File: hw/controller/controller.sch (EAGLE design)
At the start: 57 parts, among them J1 MF-CON-MICROUSB-RIGHT, P1 B6B-PH-SM4-TB(LF)(SN), Q1 TPN1R603PL, Q2 TPN1R603PL, Q3 TPN1R603PL, Q4 TPN1R603PL, Q5 TPN1R603PL, Q6 TPN1R603PL, U1 STM32F4R_64PIN, U2 DRV8323RS, U3 AS5147, U4 MAX13431E

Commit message: Checkpoint of controller board layout after much pin assignment
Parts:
- removed P1: B6B-PH-SM4-TB(LF)(SN), controller:B6B-PH-SM4-TB(LF)(SN)
- added D2: MF-LED-0603-GREEN, mfleds:LED_SINGLE-0603-GREEN
- added D3: MF-LED-0603-RED, mfleds:LED_SINGLE-0603-RED
- added J2: JST-ZH6, controller:JST-ZH6
- added J3, J6: PAD4, controller:PAD4
- added J4: JST-PH3SMT_VERT, controller:JST-PH3SMT_VERT
- added J5: PAD2, controller:PAD2
- added R5: 10k, mfpassives:RESISTOR_0603
- added R6, R9: 220, mfpassives:RESISTOR_0603
- J1: value MF-CON-MICROUSB-RIGHT -> JST-PH3SMT_VERT; device mfconnectors:USB_MICRO_RIGHT -> controller:JST-PH3SMT_VERT
- R3: value (none) -> 33.2k 1%; MF (none) -> Panasonic; MPN (none) -> ERJ-3EKF3322V
- R4: value (none) -> 10k 1%; MF (none) -> Panasonic; MPN (none) -> P10.0KHCT-ND
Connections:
- removed net N$1: J1.5V, U1.PA9/TIM1_2/SPI2_SCK/I2S3_CK/UART1_TX/USB_VBUS
- removed net N$3: J1.D+, U1.PA12/USART1_RTS/USB_DP
- removed net N$38: R7.P$1, R8.P$2, U1.PA0WKUP/TIM2_1/TIM5_1/UART4_TX
- removed net N$4: J1.D-, U1.PA11/TIM1_4/USB_DM
- new net I2C_ABS_SCL: J3.3, U1.PB8/TIM2_1/TIM4_3/TIM10_1/I2C1_SCL
- new net I2C_ABS_SDA: J3.2, U1.PB9/TIM2_2/TIM4_4/TIM11_1/I2C1_SDA
- new net LED1: D3.CATHODE, U1.PA11/TIM1_4/USB_DM
- new net LED2: D2.CATHODE, U1.PA12/USART1_RTS/USB_DP
- new net N$15: J1.1, J4.1, U4.A
- new net N$17: D3.ANODE, R6.P$2
- new net N$18: D2.ANODE, R9.P$2
- new net N$9: J1.2, J4.2, U4.B
- new net VBAT_SENSE: R7.P$1, R8.P$2, U1.PC1/SPI3_MOSI/I2S3_SD/SPI2_MOSI/I2S2_SD
- new net VTEMP: J5.2, R5.P$1, U1.PC0
- net +3V3: now also J2.6, J3.1, J5.1, J6.1, R6.P$1, R9.P$1; no longer P1.6
- net AS5047_A: now also U1.PC6/TIM3_1/TIM8_1/I2S2_MCK/UART6_RX
- net AS5047_B: now also U1.PC7/TIM3_2/TIM8_2/SPI2_SCK/I2S2_CK/I2S3_MCK/UART6_RX
- net AS5047_CS: now also U1.PB12; no longer U1.PC15
- net AS5047_MISO: now also U1.PB14/TIM1_2N/TIM8_2N/SPI2_MISO/TIM12_1/USB_HS_DM; no longer U1.PC11/SPI3_MISO/UART3_RX/UART4_RX
- net AS5047_MOSI: now also U1.PB15/TIM1_3N/TIM8_3N/SPI2_MOSI/I2S2_SD/TIM12_2/USB_HS_DP; no longer U1.PC12/I2C2_SDA/SPI3_MOSI/I2S3_SD/UART3_CK/UART5_TX
- net AS5047_SCK: now also U1.PB13/TIM1_1N/SPI2_SCK/I2S2_CK; no longer U1.PC10/SPI3_SCK/I2S3_CK/UART3_TX/UART4_TX
- net CUR1: now also U1.PC4/I2S1_MCK; no longer U1.PC0
- net CUR2: now also U1.PC5/UART3_RX; no longer U1.PC1/SPI3_MOSI/I2S3_SD/SPI2_MOSI/I2S2_SD
- net CUR3: now also U1.PB0/TIM1_2N/TIM3_3/TIM8_2N/SPI3_MOSI/I2S3_SD/UART4_CTS; no longer U1.PC2/SPI2_MISO
- net DEBUG_RX: now also J6.3, U1.PC11/SPI3_MISO/UART3_RX/UART4_RX; no longer U1.PA3/TIM2_4/TIM5_4/TIM9_2/UART2_RX
- net DEBUG_TX: now also J6.2, U1.PC10/SPI3_SCK/I2S3_CK/UART3_TX/UART4_TX; no longer U1.PA2/TIM2_3/TIM5_3/TIM9_1/UART2_TX
- net DRV8323_CS: now also U1.PA4; no longer U1.PA8/TIM1_1/I2C3_SCL
- net GND: now also J1.3, J2.4, J3.4, J4.3, J6.4, R5.P$2; no longer J1.GND, J1.SLD, P1.4
- net MOTOR1: now also U1.PA0WKUP/TIM2_1/TIM5_1/UART4_TX; no longer U1.PC6/TIM3_1/TIM8_1/I2S2_MCK/UART6_RX
- net MOTOR2: now also U1.PA1/TIM2_2/TIM5_2/UART4_RX; no longer U1.PC7/TIM3_2/TIM8_2/SPI2_SCK/I2S2_CK/I2S3_MCK/UART6_RX
- net MOTOR3: now also U1.PA2/TIM2_3/TIM5_3/TIM9_1/UART2_TX; no longer U1.PC8/TIM3_3/TIM8_3/UART6_CK
- net MOTOR_ENABLE: now also U1.PA3/TIM2_4/TIM5_4/TIM9_2/UART2_RX; no longer U1.PC13
- net MOTOR_FAULT: now also U1.PB1/TIM1_3N/TIM3_4/TIM8_3N; no longer U1.PD2
- net MOTOR_HIZ: now also U1.PC3/SPI2_MOSI/I2S2_SD; no longer U1.PC14
- net N$24: now also J2.2; no longer P1.2
- net N$6: now also J2.5; no longer P1.5
- net N$7: now also J2.3; no longer P1.3
- net RS485_DIR: now also U1.PA8/TIM1_1/I2C3_SCL; no longer U1.PB5/TIM3_2/SPI1_MOSI/I2S1_SD/SPI3_MOSI/I2S3_SD
- net RS485_RX: now also U1.PA10/TIM1_3/USART1_RX; no longer U1.PB7/TIM4_2/I2C1_SDA/UART1_RX
- net RS485_TX: now also U1.PA9/TIM1_2/SPI2_SCK/I2S3_CK/UART1_TX/USB_VBUS; no longer U1.PB6/TIM4_1/I2C1_SCL/UART1_TX
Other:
- moved on the sheet: R7, R8

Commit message: Checkpoint after fixing board consistency errors
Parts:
- C4: device mfpassives:CAPACITOR_NP_0603 -> mfpassives:CAPACITOR_NP_0402
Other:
- moved on the sheet: R1, R2, R3, R4, R5, R6, R7, R8, R9

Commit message: Everything nominally placed within the board outline
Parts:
- added C26: 0.1uF, mfpassives:CAPACITOR_NP_0402
- added C27: 1uF, mfpassives:CAPACITOR_NP_0402
- added U$1, U$2, U$3, U$4: MOUNTM2, controller:MOUNTM2
- C10, C11, C12, C13, C2, C21, C23, C24, C25, C3, C5, C6, C8, C9: device mfpassives:CAPACITOR_NP_0603 -> mfpassives:CAPACITOR_NP_0402
- C4: HOUSEPART (none) -> 1; MPN MF-CAP-0603-0.1uF -> MF-CAP-0402-0.1uF
- R1, R2, R5, R6, R9: device mfpassives:RESISTOR_0603 -> mfpassives:RESISTOR_0402
- X1: value (none) -> 8.0MHz
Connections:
- removed net N$2: C13.P$1, C23.P$1, U2.VDRAIN, U2.VM
- net +3V3: now also C26.P$1, C27.P$1
- net GND: now also C26.P$2, C27.P$2
- net V+: now also C13.P$1, C23.P$1, U2.VDRAIN, U2.VM

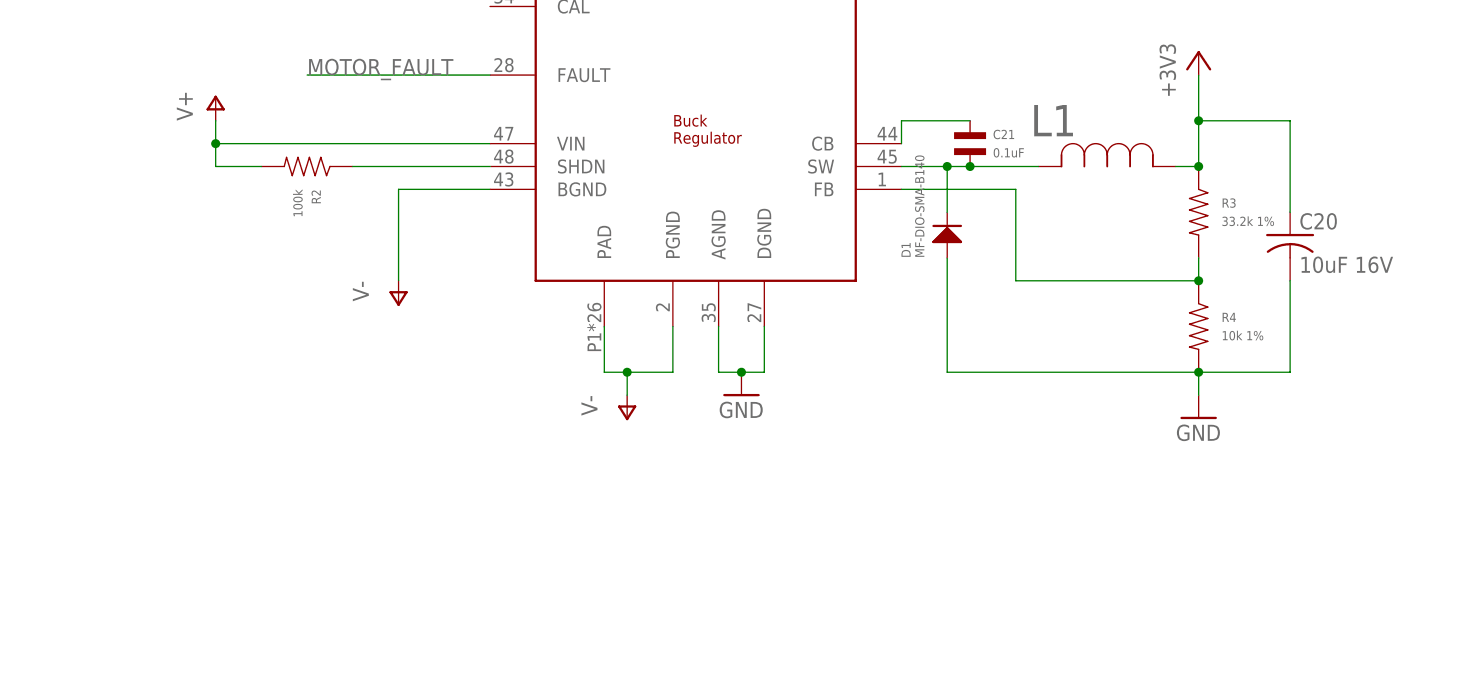
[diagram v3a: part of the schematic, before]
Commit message: Most of the power side is now routed
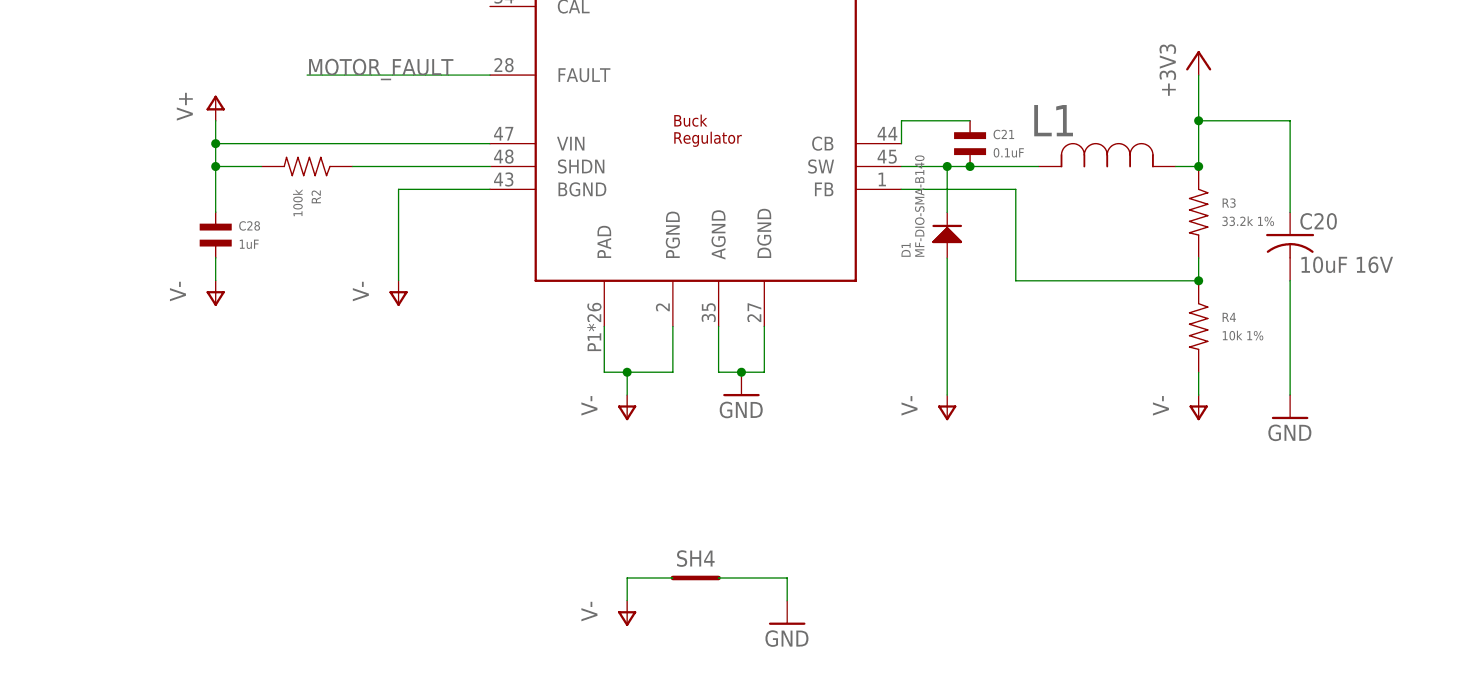
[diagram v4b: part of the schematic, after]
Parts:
- added C28: 1uF, mfpassives:CAPACITOR_NP_0402
- added SH4: SHORTBIG, shorts:SHORTBIG
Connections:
- net GND: now also SH4.P$2; no longer D1.ANODE, R4.P$2
- net V+: now also C28.P$1
- net V-: now also C28.P$2, D1.ANODE, R4.P$2, SH4.P$1
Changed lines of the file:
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@@
 </part>
 <part name="P+4" library="supply1" deviceset="V+" device=""/>
+<part name="SH4" library="shorts" deviceset="SHORT" device="BIG" value="SHORTBIG"/>
+<part name="P-5" library="supply1" deviceset="V-" device=""/>
+<part name="GND12" library="supply1" deviceset="GND" device=""/>
+<part name="P-6" library="supply1" deviceset="V-" device=""/>
+<part name="P-7" library="supply1" deviceset="V-" device=""/>
+<part name="C28" library="mfpassives" deviceset="CAPACITOR_NP" device="_0402" value="1uF">
+<attribute name="MPN" value="MF-CAP-0402-1uF"/>
+</part>
+<part name="P-8" library="supply1" deviceset="V-" device=""/>
 </parts>
 <sheets>
@@
 <attribute name="MF" x="134.62" y="-342.9" size="1.778" layer="96" display="off"/>
 </instance>
-<instance part="GND7" gate="1" x="134.62" y="-353.06"/>
+<instance part="GND7" gate="1" x="144.78" y="-353.06"/>
 <instance part="C20" gate="G$1" x="144.78" y="-332.74"/>
 <instance part="C21" gate="G$1" x="109.22" y="-322.58">
@@
 </instance>
 <instance part="P+4" gate="1" x="30.48" y="-226.06"/>
+<instance part="SH4" gate="G$1" x="78.74" y="-370.84"/>
+<instance part="P-5" gate="1" x="71.12" y="-375.92"/>
+<instance part="GND12" gate="1" x="88.9" y="-375.92"/>
+<instance part="P-6" gate="1" x="106.68" y="-353.06"/>
+<instance part="P-7" gate="1" x="134.62" y="-353.06"/>
+<instance part="C28" gate="G$1" x="25.4" y="-332.74">
+<attribute name="MPN" x="25.4" y="-332.74" size="1.778" layer="96" display="off"/>
+</instance>
+<instance part="P-8" gate="1" x="25.4" y="-340.36"/>
 </instances>
 <busses>
@@
 </segment>
 <segment>
-<pinref part="GND7" gate="1" pin="GND"/>
-<pinref part="R4" gate="G$1" pin="P$2"/>
-<wire x1="134.62" y1="-350.52" x2="134.62" y2="-347.98" width="0.1524" layer="91"/>
-<pinref part="C20" gate="G$1" pin="2"/>
-<wire x1="134.62" y1="-347.98" x2="144.78" y2="-347.98" width="0.1524" layer="91"/>
-<wire x1="144.78" y1="-347.98" x2="144.78" y2="-337.82" width="0.1524" layer="91"/>
-<junction x="134.62" y="-347.98"/>
-<pinref part="D1" gate="G$1" pin="ANODE"/>
-<wire x1="106.68" y1="-335.28" x2="106.68" y2="-347.98" width="0.1524" layer="91"/>
-<wire x1="106.68" y1="-347.98" x2="134.62" y2="-347.98" width="0.1524" layer="91"/>
-</segment>
-<segment>
 <pinref part="C24" gate="G$1" pin="P$1"/>
 <pinref part="GND8" gate="1" pin="GND"/>
@@
 <pinref part="GND3" gate="1" pin="GND"/>
 <wire x1="7.62" y1="-149.86" x2="7.62" y2="-154.94" width="0.1524" layer="91"/>
+</segment>
+<segment>
+<pinref part="GND12" gate="1" pin="GND"/>
+<wire x1="88.9" y1="-373.38" x2="88.9" y2="-370.84" width="0.1524" layer="91"/>
+<pinref part="SH4" gate="G$1" pin="P$2"/>
+<wire x1="88.9" y1="-370.84" x2="81.28" y2="-370.84" width="0.1524" layer="91"/>
+</segment>
+<segment>
+<pinref part="C20" gate="G$1" pin="2"/>
+<wire x1="144.78" y1="-350.52" x2="144.78" y2="-337.82" width="0.1524" layer="91"/>
+<pinref part="GND7" gate="1" pin="GND"/>
 </segment>
 </net>
@@
 <wire x1="25.4" y1="-325.12" x2="25.4" y2="-322.58" width="0.1524" layer="91"/>
 <junction x="25.4" y="-322.58"/>
+<pinref part="C28" gate="G$1" pin="P$1"/>
+<wire x1="25.4" y1="-330.2" x2="25.4" y2="-325.12" width="0.1524" layer="91"/>
+<junction x="25.4" y="-325.12"/>
 </segment>
 <segment>
@@
 <wire x1="45.72" y1="-327.66" x2="55.88" y2="-327.66" width="0.1524" layer="91"/>
 </segment>
-</net>
+<segment>
+<pinref part="P-5" gate="1" pin="V-"/>
+<wire x1="71.12" y1="-373.38" x2="71.12" y2="-370.84" width="0.1524" layer="91"/>
+<pinref part="SH4" gate="G$1" pin="P$1"/>
+<wire x1="71.12" y1="-370.84" x2="76.2" y2="-370.84" width="0.1524" layer="91"/>
+</segment>
+<segment>
+<pinref part="D1" gate="G$1" pin="ANODE"/>
+<wire x1="106.68" y1="-335.28" x2="106.68" y2="-350.52" width="0.1524" layer="91"/>
+<pinref part="P-6" gate="1" pin="V-"/>
+</segment>
+<segment>
+<pinref part="R4" gate="G$1" pin="P$2"/>
+<pinref part="P-7" gate="1" pin="V-"/>
+<wire x1="134.62" y1="-347.98" x2="134.62" y2="-350.52" width="0.1524" layer="91"/>
+</segment>
+<segment>
+<pinref part="P-8" gate="1" pin="V-"/>
+<pinref part="C28" gate="G$1" pin="P$2"/>
+<wire x1="25.4" y1="-337.82" x2="25.4" y2="-335.28" width="0.1524" layer="91"/>
+</segment>
+</net>

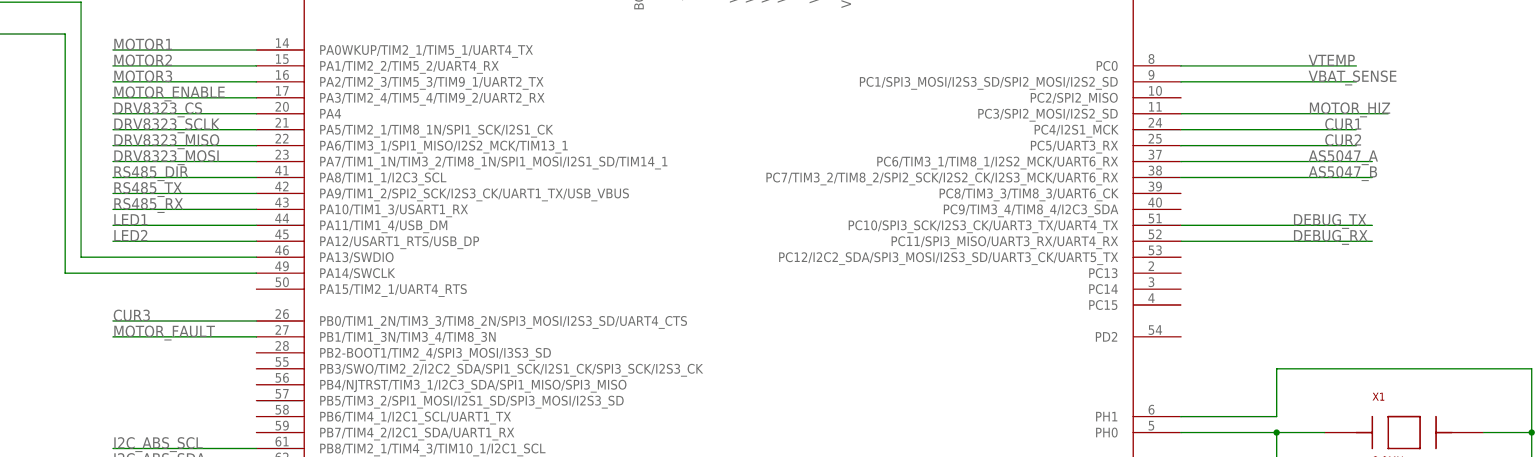
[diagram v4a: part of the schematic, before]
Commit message: Nominally all power is routed
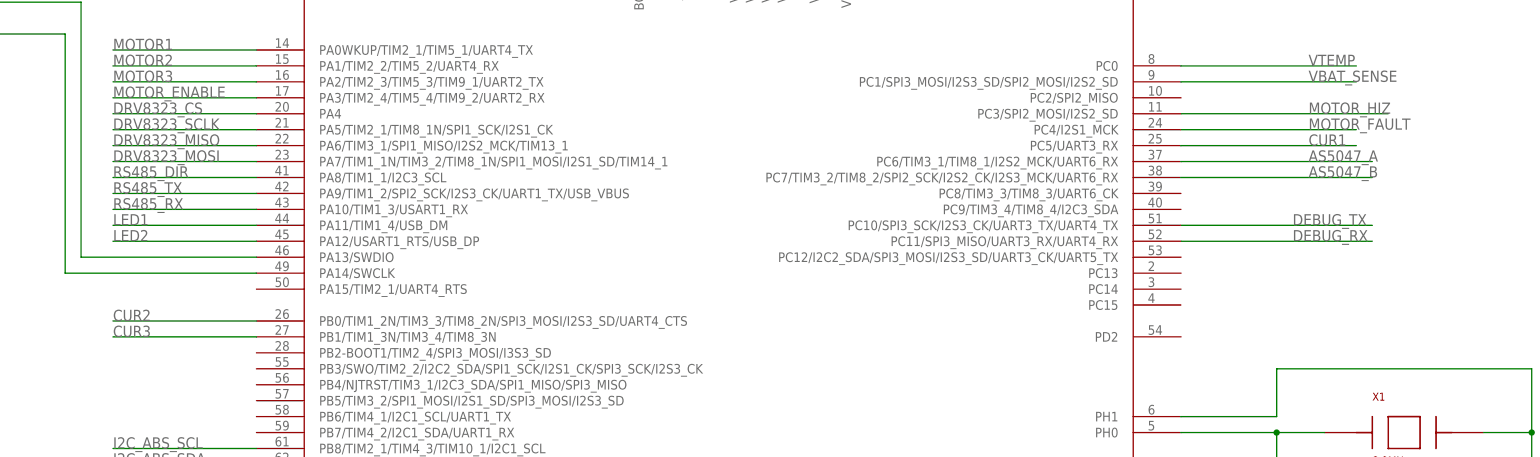
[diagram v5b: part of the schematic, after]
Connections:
- net CUR1: now also U1.PC5/UART3_RX; no longer U1.PC4/I2S1_MCK
- net CUR2: now also U1.PB0/TIM1_2N/TIM3_3/TIM8_2N/SPI3_MOSI/I2S3_SD/UART4_CTS; no longer U1.PC5/UART3_RX
- net CUR3: now also U1.PB1/TIM1_3N/TIM3_4/TIM8_3N; no longer U1.PB0/TIM1_2N/TIM3_3/TIM8_2N/SPI3_MOSI/I2S3_SD/UART4_CTS
- net MOTOR_FAULT: now also U1.PC4/I2S1_MCK; no longer U1.PB1/TIM1_3N/TIM3_4/TIM8_3N
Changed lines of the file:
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@@
 </segment>
 <segment>
-<pinref part="U1" gate="G$1" pin="PC4/I2S1_MCK"/>
-<wire x1="167.64" y1="63.5" x2="195.58" y2="63.5" width="0.1524" layer="91"/>
-<label x="190.5" y="63.5" size="1.778" layer="95"/>
+<pinref part="U1" gate="G$1" pin="PC5/UART3_RX"/>
+<wire x1="167.64" y1="60.96" x2="195.58" y2="60.96" width="0.1524" layer="91"/>
+<label x="187.96" y="60.96" size="1.778" layer="95"/>
 </segment>
 </net>
@@
 </segment>
 <segment>
-<pinref part="U1" gate="G$1" pin="PC5/UART3_RX"/>
-<wire x1="167.64" y1="60.96" x2="195.58" y2="60.96" width="0.1524" layer="91"/>
-<label x="190.5" y="60.96" size="1.778" layer="95"/>
+<pinref part="U1" gate="G$1" pin="PB0/TIM1_2N/TIM3_3/TIM8_2N/SPI3_MOSI/I2S3_SD/UART4_CTS"/>
+<wire x1="20.32" y1="33.02" x2="-2.54" y2="33.02" width="0.1524" layer="91"/>
+<label x="-2.54" y="33.02" size="1.778" layer="95"/>
 </segment>
 </net>
@@
 </segment>
 <segment>
-<pinref part="U1" gate="G$1" pin="PB0/TIM1_2N/TIM3_3/TIM8_2N/SPI3_MOSI/I2S3_SD/UART4_CTS"/>
-<wire x1="20.32" y1="33.02" x2="-2.54" y2="33.02" width="0.1524" layer="91"/>
-<label x="-2.54" y="33.02" size="1.778" layer="95"/>
+<pinref part="U1" gate="G$1" pin="PB1/TIM1_3N/TIM3_4/TIM8_3N"/>
+<wire x1="20.32" y1="30.48" x2="-2.54" y2="30.48" width="0.1524" layer="91"/>
+<label x="-2.54" y="30.48" size="1.778" layer="95"/>
 </segment>
 </net>
@@
 </segment>
 <segment>
-<pinref part="U1" gate="G$1" pin="PB1/TIM1_3N/TIM3_4/TIM8_3N"/>
-<wire x1="20.32" y1="30.48" x2="-2.54" y2="30.48" width="0.1524" layer="91"/>
-<label x="-2.54" y="30.48" size="1.778" layer="95"/>
-</segment>
-</net>
+<pinref part="U1" gate="G$1" pin="PC4/I2S1_MCK"/>
+<wire x1="167.64" y1="63.5" x2="195.58" y2="63.5" width="0.1524" layer="91"/>
+<label x="187.96" y="63.5" size="1.778" layer="95"/>
+</segment>
+</net>
